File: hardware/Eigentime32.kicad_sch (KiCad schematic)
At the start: 0 parts

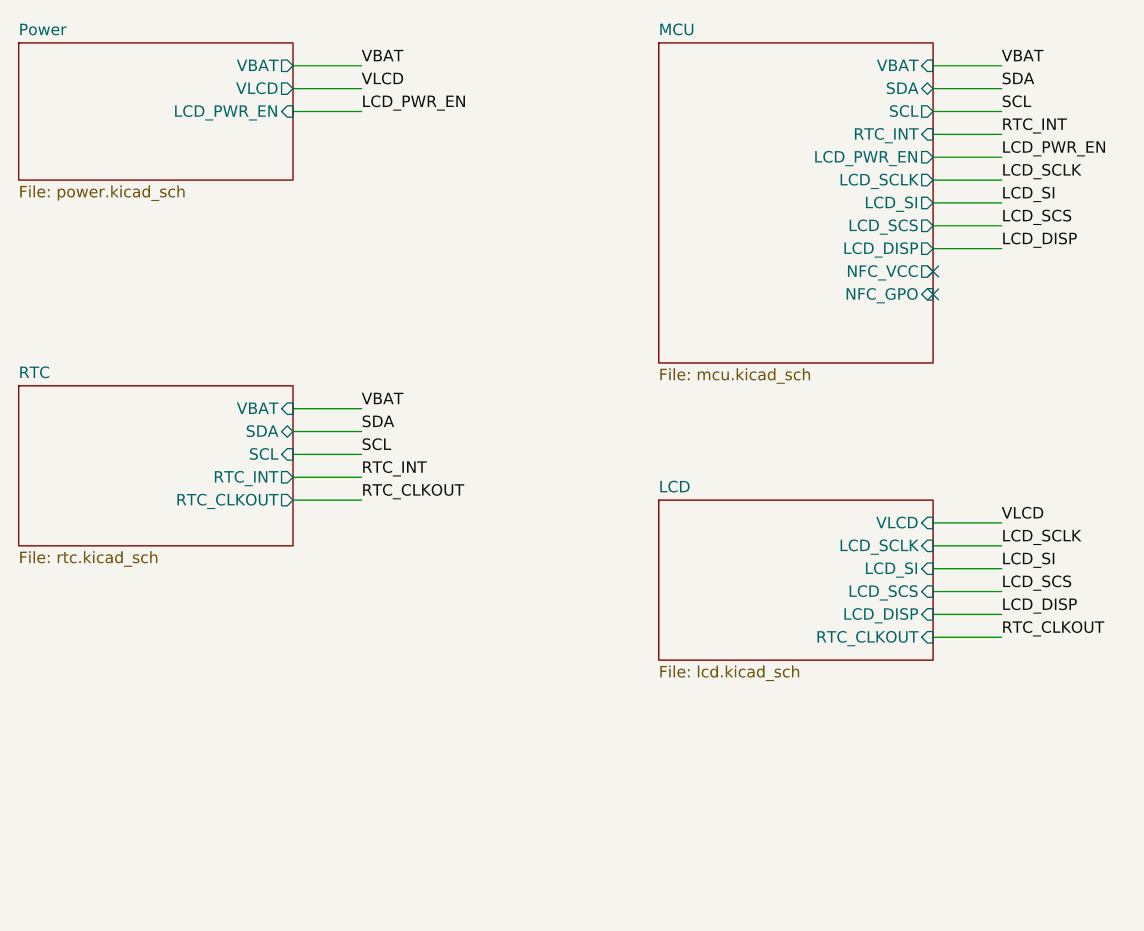
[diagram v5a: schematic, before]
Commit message: Add NFC sheet
ST25DV04KC-IE6C3 (UFDFPN8, 2x3 mm; the ST25DV04K is NRND) with VCC
from MCU PB0, 100 nF decoupling and a 100k pull-down so VCC never
floats (KC errata). Open-drain GPO pulled up to always-on VBAT through
1M; it works from RF power alone, so a phone tap wakes the MCU.
I2C joins the shared bus. The exposed pad is left floating per ST.

Antenna: placeholder footprint for a 39 mm OD, 7-8 turn,
0.15/0.15 mm PCB loop (target ~4.8 uH with the 28.5 pF internal
tuning cap) plus a DNP 0402 tuning cap across AC0/AC1.

Project symbol for the KC part with VCC typed passive (it is fed from
a GPIO). The last root-sheet no-connects are gone. ERC is clean with
all severities enabled.

Co-Authored-By: Claude Opus 5.5 (1M context) <noreply@anthropic.com>
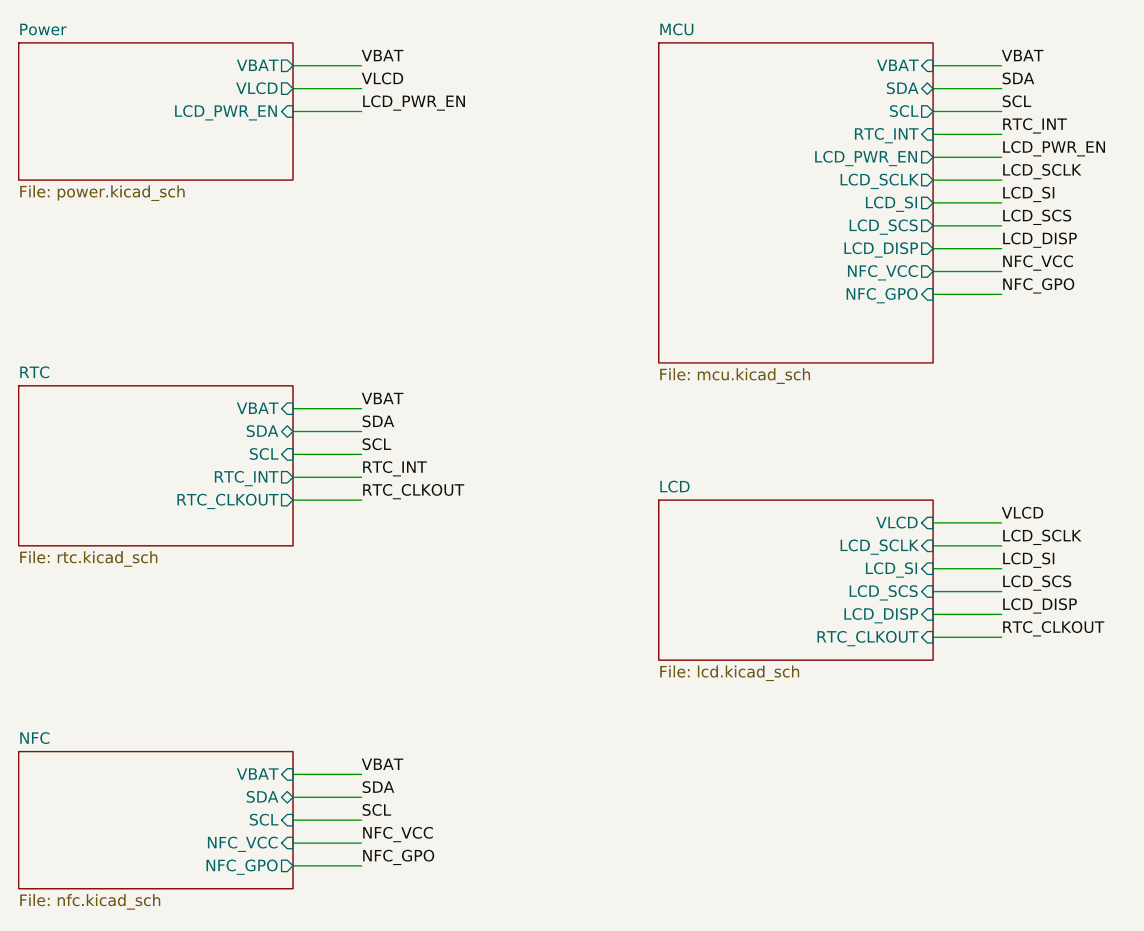
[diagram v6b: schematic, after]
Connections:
- no-connect marks 2 -> 0
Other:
- added sheet NFC (nfc.kicad_sch)
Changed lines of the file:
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@@
 		(instances (project "Eigentime32" (path "/6b2f6c1e-3a0d-4e6b-9a51-0e5c2f3d7a10" (page "5"))))
+	)
+	(sheet (at 50.8 129.54) (size 30.48 15.24) (exclude_from_sim no) (in_bom yes) (on_board yes) (dnp no)
+		(fields_autoplaced yes)
+		(stroke (width 0.1524) (type solid))
+		(fill (color 0 0 0 0.0000))
+		(property "Sheetname" "NFC" (at 50.8 128.8284 0) (effects (font (size 1.27 1.27)) (justify left bottom)))
+		(property "Sheetfile" "nfc.kicad_sch" (at 50.8 145.3646 0) (effects (font (size 1.27 1.27)) (justify left top)))
+		(pin "VBAT" input (at 81.28 132.08 0) (effects (font (size 1.27 1.27)) (justify right)))
+		(pin "SDA" bidirectional (at 81.28 134.62 0) (effects (font (size 1.27 1.27)) (justify right)))
+		(pin "SCL" input (at 81.28 137.16 0) (effects (font (size 1.27 1.27)) (justify right)))
+		(pin "NFC_VCC" input (at 81.28 139.7 0) (effects (font (size 1.27 1.27)) (justify right)))
+		(pin "NFC_GPO" output (at 81.28 142.24 0) (effects (font (size 1.27 1.27)) (justify right)))
+		(instances (project "Eigentime32" (path "/6b2f6c1e-3a0d-4e6b-9a51-0e5c2f3d7a10" (page "6"))))
 	)
 	(wire (pts (xy 81.28 53.34) (xy 88.9 53.34)) (stroke (width 0) (type default)))
@@
 	(wire (pts (xy 152.4 73.66) (xy 160.02 73.66)) (stroke (width 0) (type default)))
 	(label "LCD_DISP" (at 160.02 73.66 0) (effects (font (size 1.27 1.27)) (justify left bottom)))
-	(no_connect (at 152.4 76.2))
-	(no_connect (at 152.4 78.74))
+	(wire (pts (xy 152.4 76.2) (xy 160.02 76.2)) (stroke (width 0) (type default)))
+	(label "NFC_VCC" (at 160.02 76.2 0) (effects (font (size 1.27 1.27)) (justify left bottom)))
+	(wire (pts (xy 152.4 78.74) (xy 160.02 78.74)) (stroke (width 0) (type default)))
+	(label "NFC_GPO" (at 160.02 78.74 0) (effects (font (size 1.27 1.27)) (justify left bottom)))
 	(wire (pts (xy 152.4 104.14) (xy 160.02 104.14)) (stroke (width 0) (type default)))
 	(label "VLCD" (at 160.02 104.14 0) (effects (font (size 1.27 1.27)) (justify left bottom)))
@@
 	(wire (pts (xy 152.4 116.84) (xy 160.02 116.84)) (stroke (width 0) (type default)))
 	(label "RTC_CLKOUT" (at 160.02 116.84 0) (effects (font (size 1.27 1.27)) (justify left bottom)))
+	(wire (pts (xy 81.28 132.08) (xy 88.9 132.08)) (stroke (width 0) (type default)))
+	(label "VBAT" (at 88.9 132.08 0) (effects (font (size 1.27 1.27)) (justify left bottom)))
+	(wire (pts (xy 81.28 134.62) (xy 88.9 134.62)) (stroke (width 0) (type default)))
+	(label "SDA" (at 88.9 134.62 0) (effects (font (size 1.27 1.27)) (justify left bottom)))
+	(wire (pts (xy 81.28 137.16) (xy 88.9 137.16)) (stroke (width 0) (type default)))
+	(label "SCL" (at 88.9 137.16 0) (effects (font (size 1.27 1.27)) (justify left bottom)))
+	(wire (pts (xy 81.28 139.7) (xy 88.9 139.7)) (stroke (width 0) (type default)))
+	(label "NFC_VCC" (at 88.9 139.7 0) (effects (font (size 1.27 1.27)) (justify left bottom)))
+	(wire (pts (xy 81.28 142.24) (xy 88.9 142.24)) (stroke (width 0) (type default)))
+	(label "NFC_GPO" (at 88.9 142.24 0) (effects (font (size 1.27 1.27)) (justify left bottom)))
 	(sheet_instances (path "/" (page "1")))
 	(embedded_fonts no)
